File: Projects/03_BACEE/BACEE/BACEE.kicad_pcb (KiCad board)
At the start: 2 copper layers, 0 parts

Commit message: Project 3: Set design rules
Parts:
- added BT1: Battery 3V, Connector_PinHeader_2.54mm:PinHeader_1x02_P2.54mm_Vertical, F.Cu at (229.9, 95.2)
- added C1: 22pF, Diode_SMD:D_0805_2012Metric_Pad1.15x1.40mm_HandSolder, F.Cu at (260.1, 107.5)
- added C2: 22pF, Diode_SMD:D_0805_2012Metric_Pad1.15x1.40mm_HandSolder, F.Cu at (271.2, 100.7)
- added C3: 10uF, Diode_SMD:D_0805_2012Metric_Pad1.15x1.40mm_HandSolder, F.Cu at (271.2, 97.6)
- added D1: LED, LED_SMD:LED_0805_2012Metric_Pad1.15x1.40mm_HandSolder, F.Cu at (266.6, 106.9)
- added J1: Digital Pins, Connector_PinSocket_2.54mm:PinSocket_1x09_P2.54mm_Vertical, F.Cu at (208.8, 94.5)
- added J2: Serial, Connector_PinSocket_2.54mm:PinSocket_1x04_P2.54mm_Vertical, F.Cu at (218.0, 94.5)
- added J3: ICSP, Connector_PinSocket_2.54mm:PinSocket_2x03_P2.54mm_Vertical, F.Cu at (225.2, 94.5)
- added J4: I2C, Connector_PinSocket_2.54mm:PinSocket_1x04_P2.54mm_Vertical, F.Cu at (213.4, 94.5)
- added R1: 330Ohm, Resistor_SMD:R_0805_2012Metric_Pad1.20x1.40mm_HandSolder, F.Cu at (271.3, 106.6)
- added R2: 10kOhm, Resistor_SMD:R_0805_2012Metric_Pad1.20x1.40mm_HandSolder, F.Cu at (271.2, 103.6)
- added U1: DS1337_MLv1, Package_SO:SO-8_5.3x6.2mm_P1.27mm, F.Cu at (258.9, 102.1)
- added U2: 24LC1025, Package_SO:SOIJ-8_5.3x5.3mm_P1.27mm, F.Cu at (259.0, 94.7)
- added U3: 24LC1025, Package_SO:SOIJ-8_5.3x5.3mm_P1.27mm, F.Cu at (247.3, 106.4)
- added U4: ATmega328P-AU, Package_QFP:TQFP-32_7x7mm_P0.8mm, F.Cu at (247.9, 97.1)
- added Y1: Crystal 32MHz, Crystal:Crystal_SMD_MicroCrystal_CC7V-T1A-2Pin_3.2x1.5mm, F.Cu at (255.1, 107.7)
- added Y2: Crystal 16MHz, Crystal:Crystal_SMD_5032-2Pin_5.0x3.2mm_HandSoldering, F.Cu at (269.4, 93.7)
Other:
- net class PWR added: clearance 0.2, trace_width 0.3, via_dia 1, via_drill 0.6

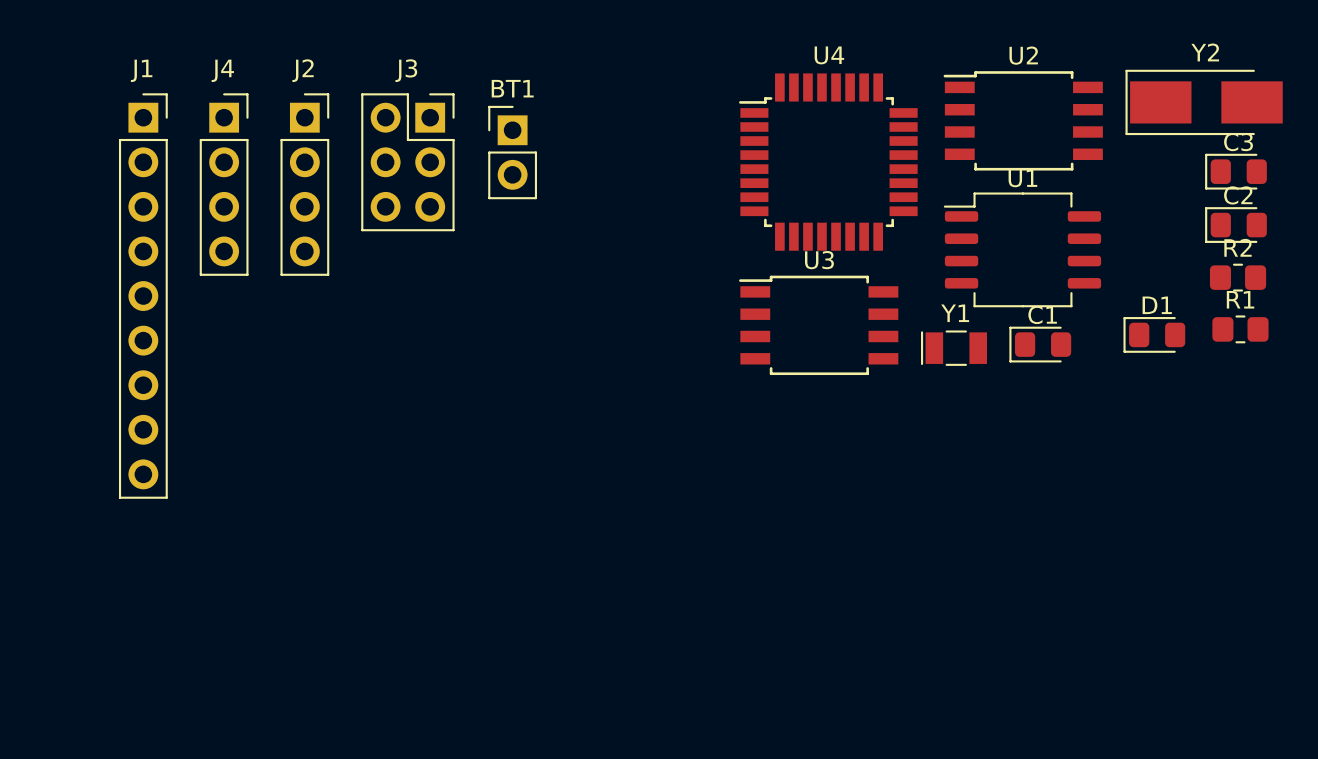
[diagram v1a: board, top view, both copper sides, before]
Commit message: Project 3: Complete placement of footprints
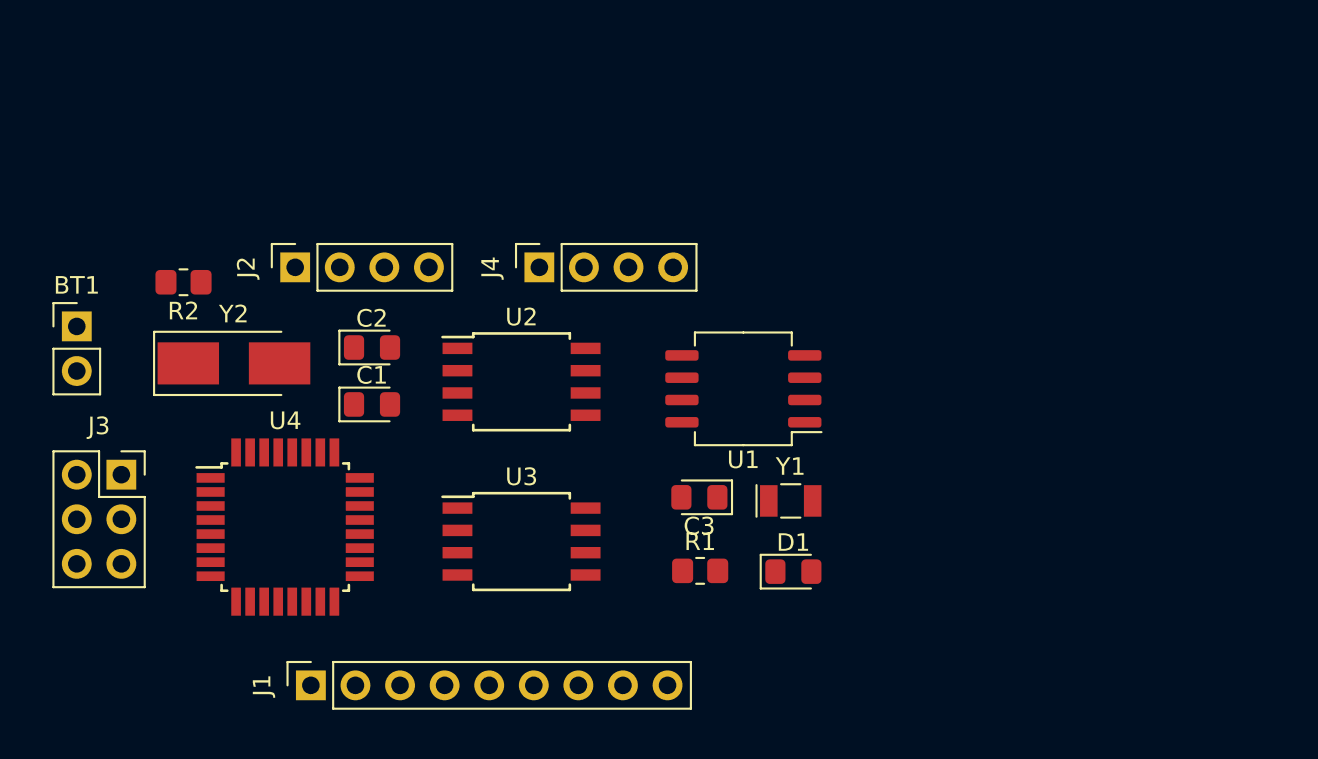
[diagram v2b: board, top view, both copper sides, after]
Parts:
- moved R2 60.1 mm to (211.1, 103.9), turned to 180 degrees
- moved Y2 57.4 mm to (214.0, 108.5)
- moved C2 49.9 mm to (221.9, 107.6)
- moved C1 38.4 mm to (221.9, 110.9)
- moved U4 37.3 mm to (216.9, 117.9)
- moved C3 35.9 mm to (240.5, 116.2), turned to 180 degrees
- moved J1 33.7 mm to (218.4, 126.9), turned to 90 degrees
- moved R1 33.7 mm to (240.6, 120.4)
- moved U2 32.2 mm to (230.4, 109.6)
- moved BT1 27.2 mm to (205.0, 106.4)
- moved J3 26.9 mm to (207.6, 114.9)
- moved D1 24.7 mm to (245.9, 120.4)
- moved U3 21.0 mm to (230.4, 118.7)
- moved J4 19.9 mm to (231.4, 103.1), turned to 90 degrees
- moved U1 17.8 mm to (243.0, 110.0), turned to 180 degrees
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
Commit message: Project 3: Create outline and mounting holes and rearrange U2 and U3
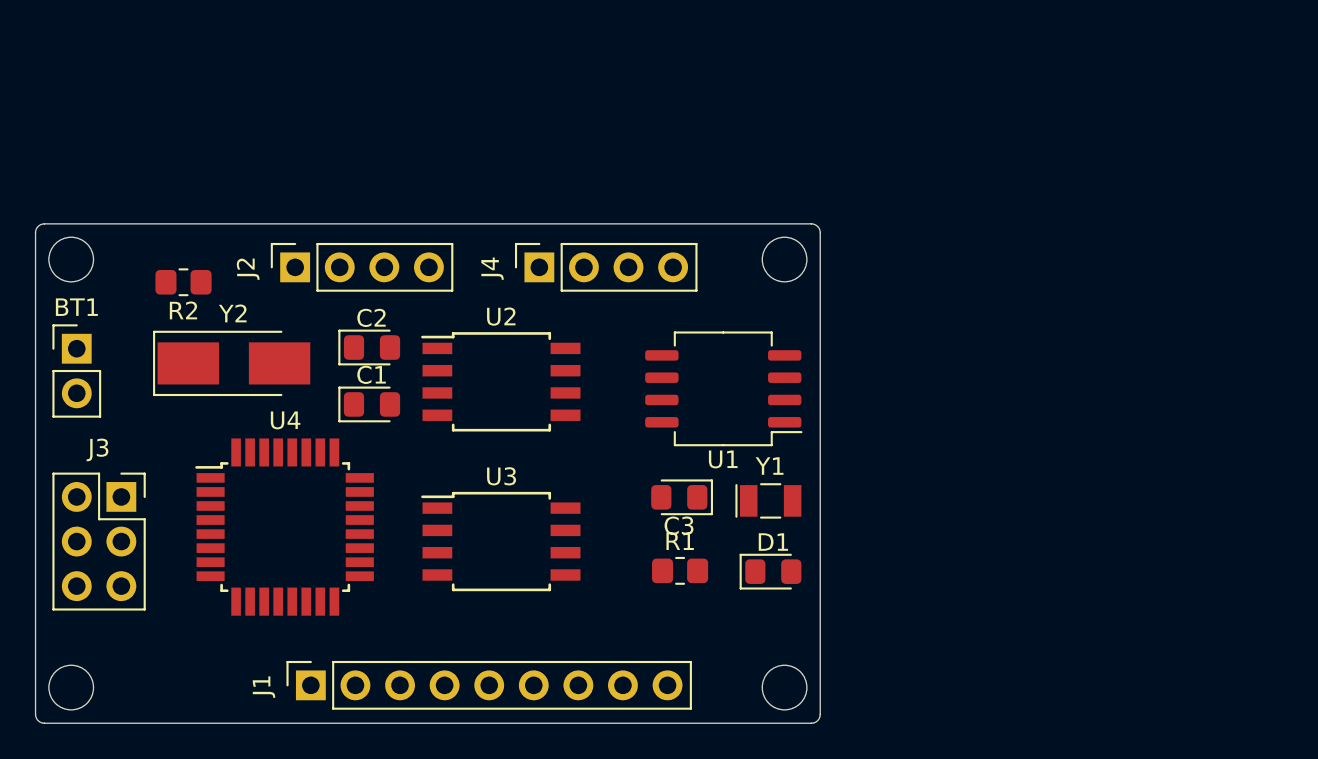
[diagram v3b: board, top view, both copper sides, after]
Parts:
- moved BT1 1.27 mm to (205.0, 107.7)
- moved J3 1.27 mm to (207.6, 116.1)
- moved D1 1.14 mm to (244.7, 120.4)
- moved R1 1.14 mm to (239.4, 120.4)
- moved U1 1.14 mm to (241.9, 110.0)
- moved Y1 1.14 mm to (244.6, 116.4)
- moved C3 1.14 mm to (239.4, 116.2)
- moved U2 1.14 mm to (229.2, 109.6)
- moved U3 1.14 mm to (229.2, 118.7)
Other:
- board outline added: 44.7 x 28.4 mm
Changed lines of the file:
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@@
   (general
     (thickness 1.6)
-    (drawings 0)
+    (drawings 12)
     (tracks 0)
     (zones 0)
@@
   )
   (module Connector_PinHeader_2.54mm:PinHeader_1x02_P2.54mm_Vertical (layer F.Cu)
-    (at 205.0415 106.426)
+    (at 205.0415 107.696)
     (descr "Through hole straight pin header, 1x02, 2.54mm pitch, single row")
     (tags "Through hole pin header THT 1x02 2.54mm single row")
@@
   )
   (module Diode_SMD:D_0805_2012Metric_Pad1.15x1.40mm_HandSolder (layer F.Cu)
-    (at 240.509 116.1615 180)
+    (at 239.366 116.1615 180)
     (descr "Diode SMD 0805 (2012 Metric), square (rectangular) end terminal, IPC_7351 nominal, (Body size source: https://docs.google.com/spreadsheets/d/1BsfQQcO9C6DZCsRaXUlFlo91Tg2WpOkGARC1WS5S8t0/edit?usp=sharing), generated with kicad-footprint-generator")
     (tags "diode handsolder")
@@
   )
   (module LED_SMD:LED_0805_2012Metric_Pad1.15x1.40mm_HandSolder (layer F.Cu)
-    (at 245.8645 120.396)
+    (at 244.7215 120.396)
     (descr "LED SMD 0805 (2012 Metric), square (rectangular) end terminal, IPC_7351 nominal, (Body size source: https://docs.google.com/spreadsheets/d/1BsfQQcO9C6DZCsRaXUlFlo91Tg2WpOkGARC1WS5S8t0/edit?usp=sharing), generated with kicad-footprint-generator")
     (tags "LED handsolder")
@@
   )
   (module Connector_PinSocket_2.54mm:PinSocket_2x03_P2.54mm_Vertical (layer F.Cu)
-    (at 207.5815 114.8715)
+    (at 207.5815 116.1415)
     (descr "Through hole straight socket strip, 2x03, 2.54mm pitch, double cols (from Kicad 4.0.7), script generated")
     (tags "Through hole socket strip THT 2x03 2.54mm double row")
@@
   )
   (module Resistor_SMD:R_0805_2012Metric_Pad1.20x1.40mm_HandSolder (layer F.Cu)
-    (at 240.554 120.351)
+    (at 239.411 120.351)
     (descr "Resistor SMD 0805 (2012 Metric), square (rectangular) end terminal, IPC_7351 nominal with elongated pad for handsoldering. (Body size source: IPC-SM-782 page 72, https://www.pcb-3d.com/wordpress/wp-content/uploads/ipc-sm-782a_amendment_1_and_2.pdf), generated with kicad-footprint-generator")
     (tags "resistor handsolder")
@@
   )
   (module Package_SO:SO-8_5.3x6.2mm_P1.27mm (layer F.Cu)
-    (at 243.0145 109.982 180)
+    (at 241.8715 109.982 180)
     (descr "SO, 8 Pin (https://www.ti.com/lit/ml/msop001a/msop001a.pdf), generated with kicad-footprint-generator ipc_gullwing_generator.py")
     (tags "SO SO")
@@
   )
   (module Package_SO:SOIJ-8_5.3x5.3mm_P1.27mm (layer F.Cu)
-    (at 230.378 109.582)
+    (at 229.235 109.582)
     (descr "8-Lead Plastic Small Outline (SM) - Medium, 5.28 mm Body [SOIC] (see Microchip Packaging Specification 00000049BS.pdf)")
     (tags "SOIC 1.27")
@@
   )
   (module Package_SO:SOIJ-8_5.3x5.3mm_P1.27mm (layer F.Cu)
-    (at 230.378 118.6815)
+    (at 229.235 118.6815)
     (descr "8-Lead Plastic Small Outline (SM) - Medium, 5.28 mm Body [SOIC] (see Microchip Packaging Specification 00000049BS.pdf)")
     (tags "SOIC 1.27")
@@
   )
   (module Crystal:Crystal_SMD_MicroCrystal_CC7V-T1A-2Pin_3.2x1.5mm (layer F.Cu)
-    (at 245.7145 116.3665)
+    (at 244.5715 116.3665)
     (descr "SMD Crystal MicroCrystal CC7V-T1A/CM7V-T1A series https://www.microcrystal.com/fileadmin/Media/Products/32kHz/Datasheet/CC7V-T1A.pdf, 3.2x1.5mm^2 package")
     (tags "SMD SMT crystal")
@@
     )
   )
+  (gr_circle (center 245.364 102.616) (end 245.364 101.346) (layer Edge.Cuts) (width 0.05))
+  (gr_circle (center 245.364 127) (end 245.364 125.73) (layer Edge.Cuts) (width 0.05))
+  (gr_circle (center 204.724 127) (end 204.724 125.73) (layer Edge.Cuts) (width 0.05))
+  (gr_circle (center 204.724 102.616) (end 204.724 101.346) (layer Edge.Cuts) (width 0.05))
+  (gr_line (start 203.2 129.032) (end 246.888 129.032) (layer Edge.Cuts) (width 0.05))
+  (gr_line (start 202.692 101.092) (end 202.692 128.524) (layer Edge.Cuts) (width 0.05))
+  (gr_line (start 246.888 100.584) (end 203.2 100.584) (layer Edge.Cuts) (width 0.05))
+  (gr_line (start 247.396 128.524) (end 247.396 101.092) (layer Edge.Cuts) (width 0.05))
+  (gr_arc (start 246.888 101.092) (end 247.396 101.092) (angle -90) (layer Edge.Cuts) (width 0.05))
+  (gr_arc (start 246.888 128.524) (end 246.888 129.032) (angle -90) (layer Edge.Cuts) (width 0.05))
+  (gr_arc (start 203.2 128.524) (end 202.692 128.524) (angle -90) (layer Edge.Cuts) (width 0.05))
+  (gr_arc (start 203.2 101.092) (end 203.2 100.584) (angle -90) (layer Edge.Cuts) (width 0.05))
 )

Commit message: Project 3: Place footprints closer together
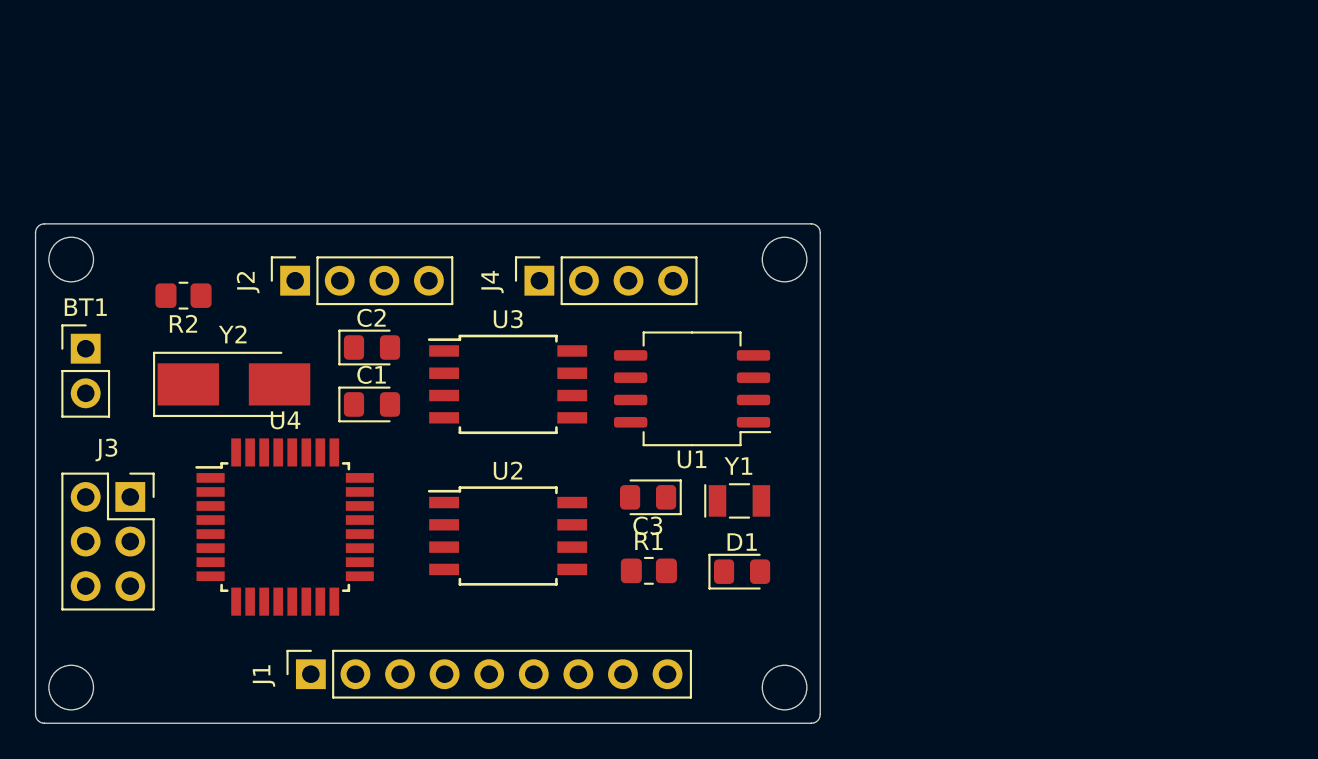
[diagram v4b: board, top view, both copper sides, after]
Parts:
- moved U3 8.96 mm to (229.6, 109.7)
- moved U2 8.79 mm to (229.6, 118.4)
- moved C3 1.78 mm to (237.6, 116.2)
- moved D1 1.78 mm to (242.9, 120.4)
- moved R1 1.78 mm to (237.6, 120.4)
- moved U1 1.78 mm to (240.1, 110.0)
- moved Y1 1.78 mm to (242.8, 116.4)
- moved Y2 1.20 mm to (214.0, 109.7)
- moved J2 0.76 mm to (217.5, 103.8)
- moved J4 0.76 mm to (231.4, 103.8)
- moved R2 0.76 mm to (211.1, 104.7)
- moved J1 0.64 mm to (218.4, 126.2)
- moved BT1 0.51 mm to (205.5, 107.7)
- moved J3 0.51 mm to (208.1, 116.1)
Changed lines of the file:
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@@
   )
   (module Connector_PinHeader_2.54mm:PinHeader_1x02_P2.54mm_Vertical (layer F.Cu)
-    (at 205.0415 107.696)
+    (at 205.5495 107.696)
     (descr "Through hole straight pin header, 1x02, 2.54mm pitch, single row")
     (tags "Through hole pin header THT 1x02 2.54mm single row")
@@
   )
   (module Diode_SMD:D_0805_2012Metric_Pad1.15x1.40mm_HandSolder (layer F.Cu)
-    (at 239.366 116.1615 180)
+    (at 237.588 116.1615 180)
     (descr "Diode SMD 0805 (2012 Metric), square (rectangular) end terminal, IPC_7351 nominal, (Body size source: https://docs.google.com/spreadsheets/d/1BsfQQcO9C6DZCsRaXUlFlo91Tg2WpOkGARC1WS5S8t0/edit?usp=sharing), generated with kicad-footprint-generator")
     (tags "diode handsolder")
@@
   )
   (module LED_SMD:LED_0805_2012Metric_Pad1.15x1.40mm_HandSolder (layer F.Cu)
-    (at 244.7215 120.396)
+    (at 242.9435 120.396)
     (descr "LED SMD 0805 (2012 Metric), square (rectangular) end terminal, IPC_7351 nominal, (Body size source: https://docs.google.com/spreadsheets/d/1BsfQQcO9C6DZCsRaXUlFlo91Tg2WpOkGARC1WS5S8t0/edit?usp=sharing), generated with kicad-footprint-generator")
     (tags "LED handsolder")
@@
   )
   (module Connector_PinSocket_2.54mm:PinSocket_1x09_P2.54mm_Vertical (layer F.Cu)
-    (at 218.3765 126.873 90)
+    (at 218.3765 126.238 90)
     (descr "Through hole straight socket strip, 1x09, 2.54mm pitch, single row (from Kicad 4.0.7), script generated")
     (tags "Through hole socket strip THT 1x09 2.54mm single row")
@@
   )
   (module Connector_PinSocket_2.54mm:PinSocket_1x04_P2.54mm_Vertical (layer F.Cu)
-    (at 217.48275 103.0605 90)
+    (at 217.48275 103.8225 90)
     (descr "Through hole straight socket strip, 1x04, 2.54mm pitch, single row (from Kicad 4.0.7), script generated")
     (tags "Through hole socket strip THT 1x04 2.54mm single row")
@@
   )
   (module Connector_PinSocket_2.54mm:PinSocket_2x03_P2.54mm_Vertical (layer F.Cu)
-    (at 207.5815 116.1415)
+    (at 208.0895 116.1415)
     (descr "Through hole straight socket strip, 2x03, 2.54mm pitch, double cols (from Kicad 4.0.7), script generated")
     (tags "Through hole socket strip THT 2x03 2.54mm double row")
@@
   )
   (module Connector_PinSocket_2.54mm:PinSocket_1x04_P2.54mm_Vertical (layer F.Cu)
-    (at 231.394 103.0605 90)
+    (at 231.394 103.8225 90)
     (descr "Through hole straight socket strip, 1x04, 2.54mm pitch, single row (from Kicad 4.0.7), script generated")
     (tags "Through hole socket strip THT 1x04 2.54mm single row")
@@
   )
   (module Resistor_SMD:R_0805_2012Metric_Pad1.20x1.40mm_HandSolder (layer F.Cu)
-    (at 239.411 120.351)
+    (at 237.633 120.351)
     (descr "Resistor SMD 0805 (2012 Metric), square (rectangular) end terminal, IPC_7351 nominal with elongated pad for handsoldering. (Body size source: IPC-SM-782 page 72, https://www.pcb-3d.com/wordpress/wp-content/uploads/ipc-sm-782a_amendment_1_and_2.pdf), generated with kicad-footprint-generator")
     (tags "resistor handsolder")
@@
   )
   (module Resistor_SMD:R_0805_2012Metric_Pad1.20x1.40mm_HandSolder (layer F.Cu)
-    (at 211.1215 103.9105 180)
+    (at 211.1215 104.6725 180)
     (descr "Resistor SMD 0805 (2012 Metric), square (rectangular) end terminal, IPC_7351 nominal with elongated pad for handsoldering. (Body size source: IPC-SM-782 page 72, https://www.pcb-3d.com/wordpress/wp-content/uploads/ipc-sm-782a_amendment_1_and_2.pdf), generated with kicad-footprint-generator")
     (tags "resistor handsolder")
@@
   )
   (module Package_SO:SO-8_5.3x6.2mm_P1.27mm (layer F.Cu)
-    (at 241.8715 109.982 180)
+    (at 240.0935 109.982 180)
     (descr "SO, 8 Pin (https://www.ti.com/lit/ml/msop001a/msop001a.pdf), generated with kicad-footprint-generator ipc_gullwing_generator.py")
     (tags "SO SO")
@@
   )
   (module Package_SO:SOIJ-8_5.3x5.3mm_P1.27mm (layer F.Cu)
-    (at 229.235 109.582)
+    (at 229.616 118.364)
     (descr "8-Lead Plastic Small Outline (SM) - Medium, 5.28 mm Body [SOIC] (see Microchip Packaging Specification 00000049BS.pdf)")
     (tags "SOIC 1.27")
@@
   )
   (module Package_SO:SOIJ-8_5.3x5.3mm_P1.27mm (layer F.Cu)
-    (at 229.235 118.6815)
+    (at 229.616 109.728)
     (descr "8-Lead Plastic Small Outline (SM) - Medium, 5.28 mm Body [SOIC] (see Microchip Packaging Specification 00000049BS.pdf)")
     (tags "SOIC 1.27")
@@
   )
   (module Crystal:Crystal_SMD_MicroCrystal_CC7V-T1A-2Pin_3.2x1.5mm (layer F.Cu)
-    (at 244.5715 116.3665)
+    (at 242.7935 116.3665)
     (descr "SMD Crystal MicroCrystal CC7V-T1A/CM7V-T1A series https://www.microcrystal.com/fileadmin/Media/Products/32kHz/Datasheet/CC7V-T1A.pdf, 3.2x1.5mm^2 package")
     (tags "SMD SMT crystal")
@@
   )
   (module Crystal:Crystal_SMD_5032-2Pin_5.0x3.2mm_HandSoldering (layer F.Cu)
-    (at 213.995 108.532)
+    (at 213.995 109.728)
     (descr "SMD Crystal SERIES SMD2520/2 http://www.icbase.com/File/PDF/HKC/HKC00061008.pdf, hand-soldering, 5.0x3.2mm^2 package")
     (tags "SMD SMT crystal hand-soldering")
